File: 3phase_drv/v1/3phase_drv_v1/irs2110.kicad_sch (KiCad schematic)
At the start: 4 parts, among them Q1 IRF3710, U1 IRS2110S

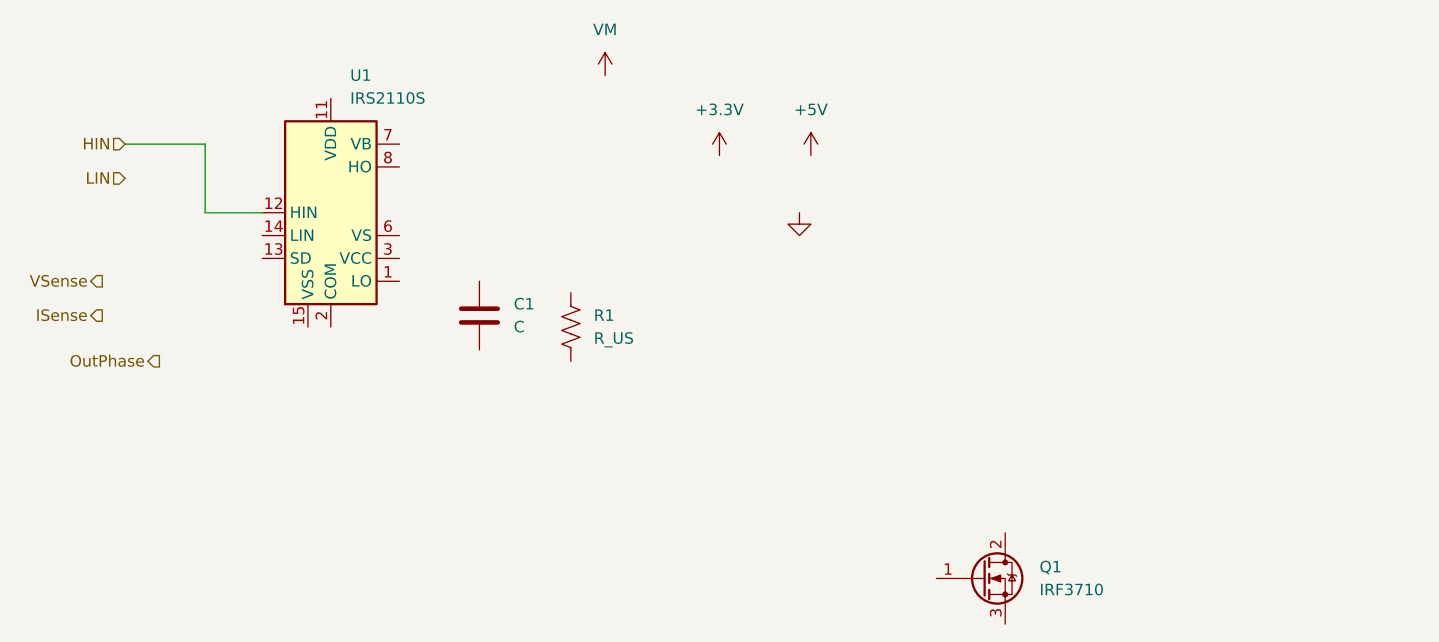
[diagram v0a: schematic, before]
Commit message: update ir2110s schematic and board layout
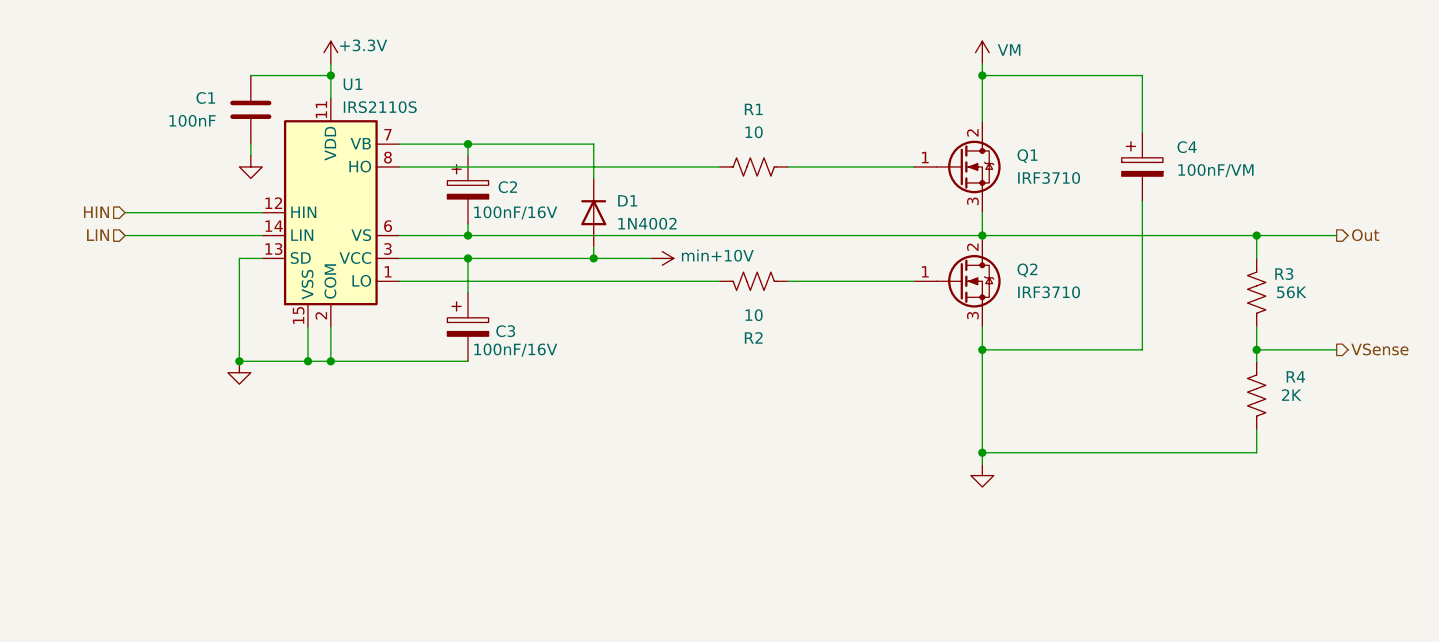
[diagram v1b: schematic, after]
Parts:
- added C2, C3: 100nF/16V, Capacitor_THT:CP_Radial_D35.0mm_P10.00mm_SnapIn, symbol Device:C_Polarized
- added C4: 100nF/VM, Capacitor_THT:CP_Radial_D35.0mm_P10.00mm_SnapIn, symbol Device:C_Polarized
- added D1: 1N4002, Diode_THT:D_DO-41_SOD81_P10.16mm_Horizontal, symbol Diode:1N4002
- added Q2: IRF3710, Package_TO_SOT_THT:TO-220-3_Horizontal_TabDown, symbol Transistor_FET:IRF3205
- added R2: 10, Resistor_SMD:R_0805_2012Metric, symbol Device:R_US
- added R3: 56K, Resistor_SMD:R_0805_2012Metric, symbol Device:R_US
- added R4: 2K, Resistor_SMD:R_0805_2012Metric, symbol Device:R_US
- C1: value C -> 100nF
- R1: value R_US -> 10
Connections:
- net +3.3V: now also C1.1, U1.11 (VDD)
- net GND: now also C1.2, U1.13 (SD), U1.15 (VSS), U1.2 (COM), C3.2, C4.2, Q2.3 (S), R4.1
- net LIN: now also U1.14 (LIN)
- net VM: now also Q1.2 (D), C4.1
- net VSense: now also R3.1, R4.2
- net at U1.1 (LO): now also R2.1
- net min+10V: now reaches U1.3 (VCC)
- net min+10V: now also C3.1, D1.2 (A)
- net Out: now reaches U1.6 (VS)
- net Out: now also Q1.3 (S), C2.2, Q2.2 (D), R3.2
- net at U1.7 (VB): now also C2.1, D1.1 (K)
- net at U1.8 (HO): now also R1.1
- net at R1.2: now also Q1.1 (G)
- new net: Q2.1 (G), R2.2
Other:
- title: (none) -> IRS2110S HL Driver
- moved on the sheet: C1, Q1, R1

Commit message: re-layout and finish routing
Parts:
- C2, C3, C4: footprint Capacitor_THT:CP_Radial_D35.0mm_P10.00mm_SnapIn -> Capacitor_THT:CP_Radial_D13.0mm_P5.00mm
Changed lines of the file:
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@@
 			)
 		)
-		(property "Footprint" "Capacitor_THT:CP_Radial_D35.0mm_P10.00mm_SnapIn"
+		(property "Footprint" "Capacitor_THT:CP_Radial_D13.0mm_P5.00mm"
 			(at 169.8752 62.23 0)
 			(hide yes)
@@
 			)
 		)
-		(property "Footprint" "Capacitor_THT:CP_Radial_D35.0mm_P10.00mm_SnapIn"
+		(property "Footprint" "Capacitor_THT:CP_Radial_D13.0mm_P5.00mm"
 			(at 94.9452 80.01 0)
 			(hide yes)
@@
 			)
 		)
-		(property "Footprint" "Capacitor_THT:CP_Radial_D35.0mm_P10.00mm_SnapIn"
+		(property "Footprint" "Capacitor_THT:CP_Radial_D13.0mm_P5.00mm"
 			(at 94.9452 64.77 0)
 			(hide yes)
